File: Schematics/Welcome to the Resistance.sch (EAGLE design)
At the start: 11 parts, among them T1 2N706, T2 2N706

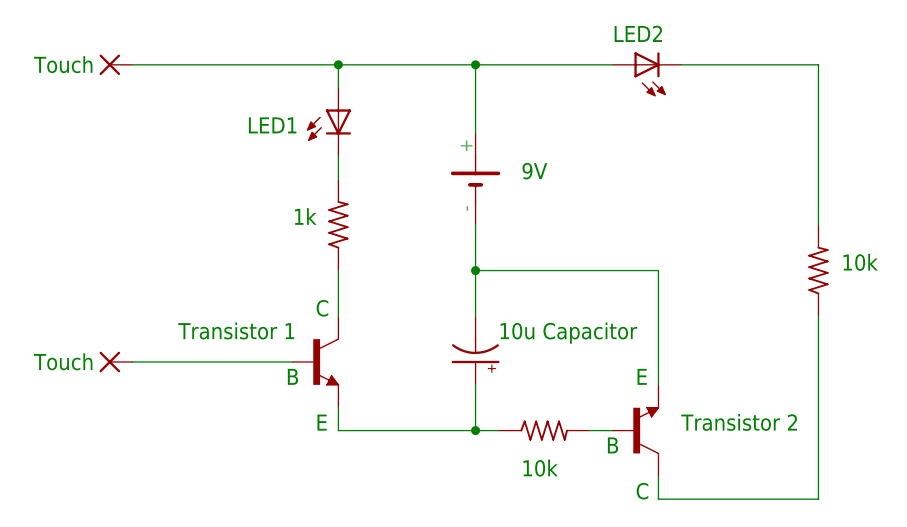
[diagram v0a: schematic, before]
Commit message: Cleaned up schematics' labeling.
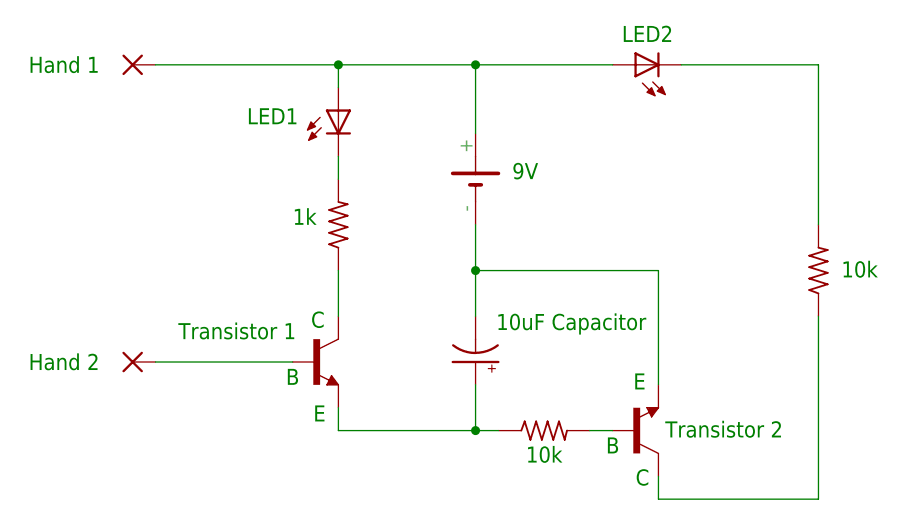
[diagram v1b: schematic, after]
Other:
- note added: "10uF Capacitor"
- note added: "Hand 1"
- note added: "Hand 2"
- note removed: "10u Capacitor"
- note removed: "Touch"
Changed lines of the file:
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@@
 <?xml version="1.0" encoding="utf-8"?>
 <!DOCTYPE eagle SYSTEM "eagle.dtd">
-<eagle version="6.6.0">
+<eagle version="9.4.2">
 <drawing>
 <settings>
 <setting alwaysvectorfont="no"/>
+<setting keepoldvectorfont="yes"/>
 <setting verticaltext="up"/>
 </settings>
@@
 <sheet>
 <plain>
-<text x="-22.86" y="73.66" size="1.778" layer="91">LED1</text>
-<text x="17.78" y="83.82" size="1.778" layer="91">LED2</text>
-<text x="43.18" y="58.42" size="1.778" layer="91">10k </text>
-<text x="7.62" y="35.56" size="1.778" layer="91">10k </text>
+<text x="-22.86" y="74.676" size="1.778" layer="91">LED1</text>
+<text x="18.796" y="83.82" size="1.778" layer="91">LED2</text>
+<text x="43.18" y="57.658" size="1.778" layer="91">10k </text>
+<text x="8.128" y="37.084" size="1.778" layer="91">10k </text>
 <text x="-17.78" y="63.5" size="1.778" layer="91">1k </text>
-<text x="5.08" y="50.8" size="1.778" layer="91">10u Capacitor</text>
-<text x="7.62" y="68.58" size="1.778" layer="91">9V</text>
+<text x="4.826" y="51.816" size="1.778" layer="91">10uF Capacitor</text>
+<text x="6.604" y="68.58" size="1.778" layer="91">9V</text>
 <text x="-30.48" y="50.8" size="1.778" layer="91">Transistor 1</text>
-<text x="25.4" y="40.64" size="1.778" layer="91">Transistor 2</text>
-<text x="-15.24" y="40.64" size="1.778" layer="91">E</text>
-<text x="20.32" y="45.72" size="1.778" layer="91">E</text>
+<text x="23.622" y="39.878" size="1.778" layer="91">Transistor 2</text>
+<text x="-15.494" y="41.656" size="1.778" layer="91">E</text>
+<text x="20.066" y="45.212" size="1.778" layer="91">E</text>
 <text x="17.78" y="38.1" size="1.778" layer="91" align="bottom-center">B</text>
 <text x="-17.78" y="45.72" size="1.778" layer="91" align="bottom-center">B</text>
-<text x="-15.24" y="53.34" size="1.778" layer="91">C</text>
-<text x="20.32" y="33.02" size="1.778" layer="91">C</text>
-<text x="-43.18" y="81.28" size="1.778" layer="91" align="center">Touch</text>
-<text x="-43.18" y="48.26" size="1.778" layer="91" align="center">Touch</text>
+<text x="-15.748" y="52.07" size="1.778" layer="91">C</text>
+<text x="20.32" y="34.544" size="1.778" layer="91">C</text>
+<text x="-43.18" y="81.28" size="1.778" layer="91" align="center">Hand 1</text>
+<text x="-43.18" y="48.26" size="1.778" layer="91" align="center">Hand 2</text>
 </plain>
 <instances>
@@
 <attribute name="VALUE" x="1.524" y="52.451" size="1.778" layer="96" rot="R180"/>
 </instance>
-<instance part="PAD1" gate="P" x="-38.1" y="81.28" smashed="yes">
-<attribute name="VALUE" x="-39.243" y="77.978" size="1.778" layer="96"/>
+<instance part="PAD1" gate="P" x="-35.56" y="81.28" smashed="yes">
+<attribute name="VALUE" x="-36.703" y="77.978" size="1.778" layer="96"/>
 </instance>
-<instance part="PAD2" gate="P" x="-38.1" y="48.26" smashed="yes">
-<attribute name="VALUE" x="-39.243" y="44.958" size="1.778" layer="96"/>
+<instance part="PAD2" gate="P" x="-35.56" y="48.26" smashed="yes">
+<attribute name="VALUE" x="-36.703" y="44.958" size="1.778" layer="96"/>
 </instance>
 </instances>
@@
 <pinref part="LED1" gate="G$1" pin="A"/>
 <wire x1="-12.7" y1="81.28" x2="-12.7" y2="78.74" width="0.1524" layer="91"/>
-<wire x1="-12.7" y1="81.28" x2="-35.56" y2="81.28" width="0.1524" layer="91"/>
+<wire x1="-12.7" y1="81.28" x2="-33.02" y2="81.28" width="0.1524" layer="91"/>
 <pinref part="PAD1" gate="P" pin="P"/>
 <junction x="-12.7" y="81.28"/>
@@
 <segment>
 <pinref part="T1" gate="G$1" pin="B"/>
-<wire x1="-17.78" y1="48.26" x2="-35.56" y2="48.26" width="0.1524" layer="91"/>
+<wire x1="-17.78" y1="48.26" x2="-33.02" y2="48.26" width="0.1524" layer="91"/>
 <pinref part="PAD2" gate="P" pin="P"/>
 </segment>
